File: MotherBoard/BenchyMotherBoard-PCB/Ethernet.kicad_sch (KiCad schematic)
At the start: 3 parts, among them J2 LVDS-DISPLAY, U4 AM6254ATCGGAALW, U5 SiI9022ACNU

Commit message: (WIP) Finish more of the PS schematic
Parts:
- removed J2: LVDS-DISPLAY, symbol Daxxn_Displays:Generic-Display-LVDS
- removed U4: AM6254ATCGGAALW, Daxxn_Packages:ALW0425A-BGA-425-13x13mm, symbol Daxxn_TIMicros:AM6254ATCGGAALW
- removed U5: SiI9022ACNU, Package_DFN_QFN:QFN-72-1EP_10x10mm_P0.5mm_EP6x6mm, symbol Daxxn_IC:SiI9022ACNU
- added U4: AM6254ATCGGAALW, Daxxn_Packages:ALW0425A-BGA-425-13x13mm, symbol Daxxn_TIMicros:AM6254ATCGGAALW

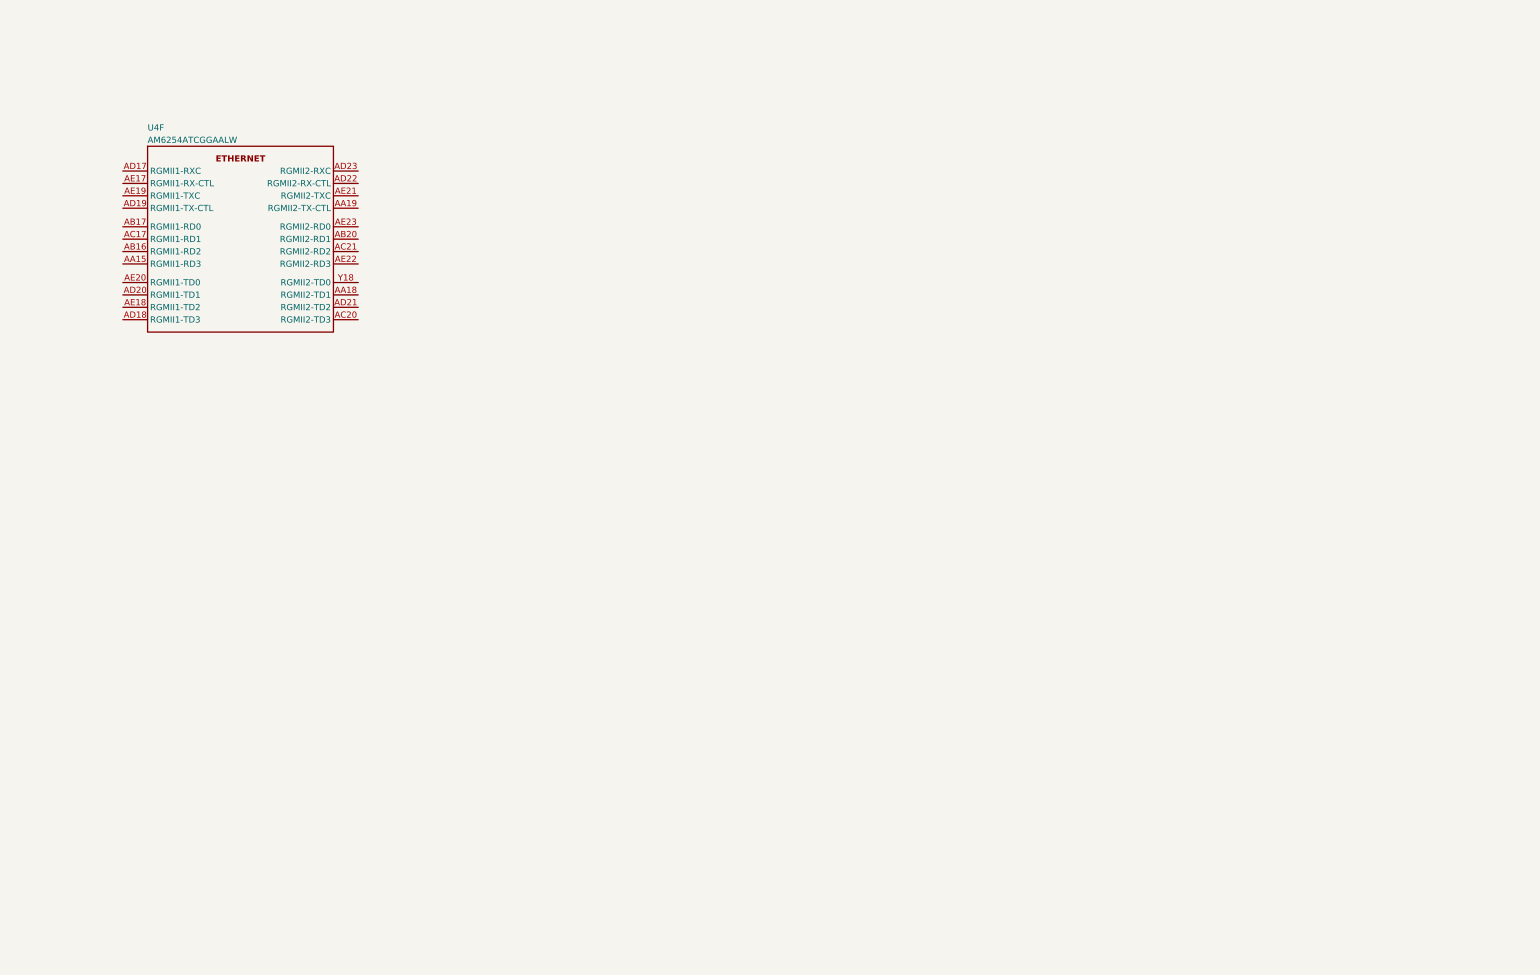
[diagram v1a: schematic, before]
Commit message: (WIP) More work on power supply sequencing
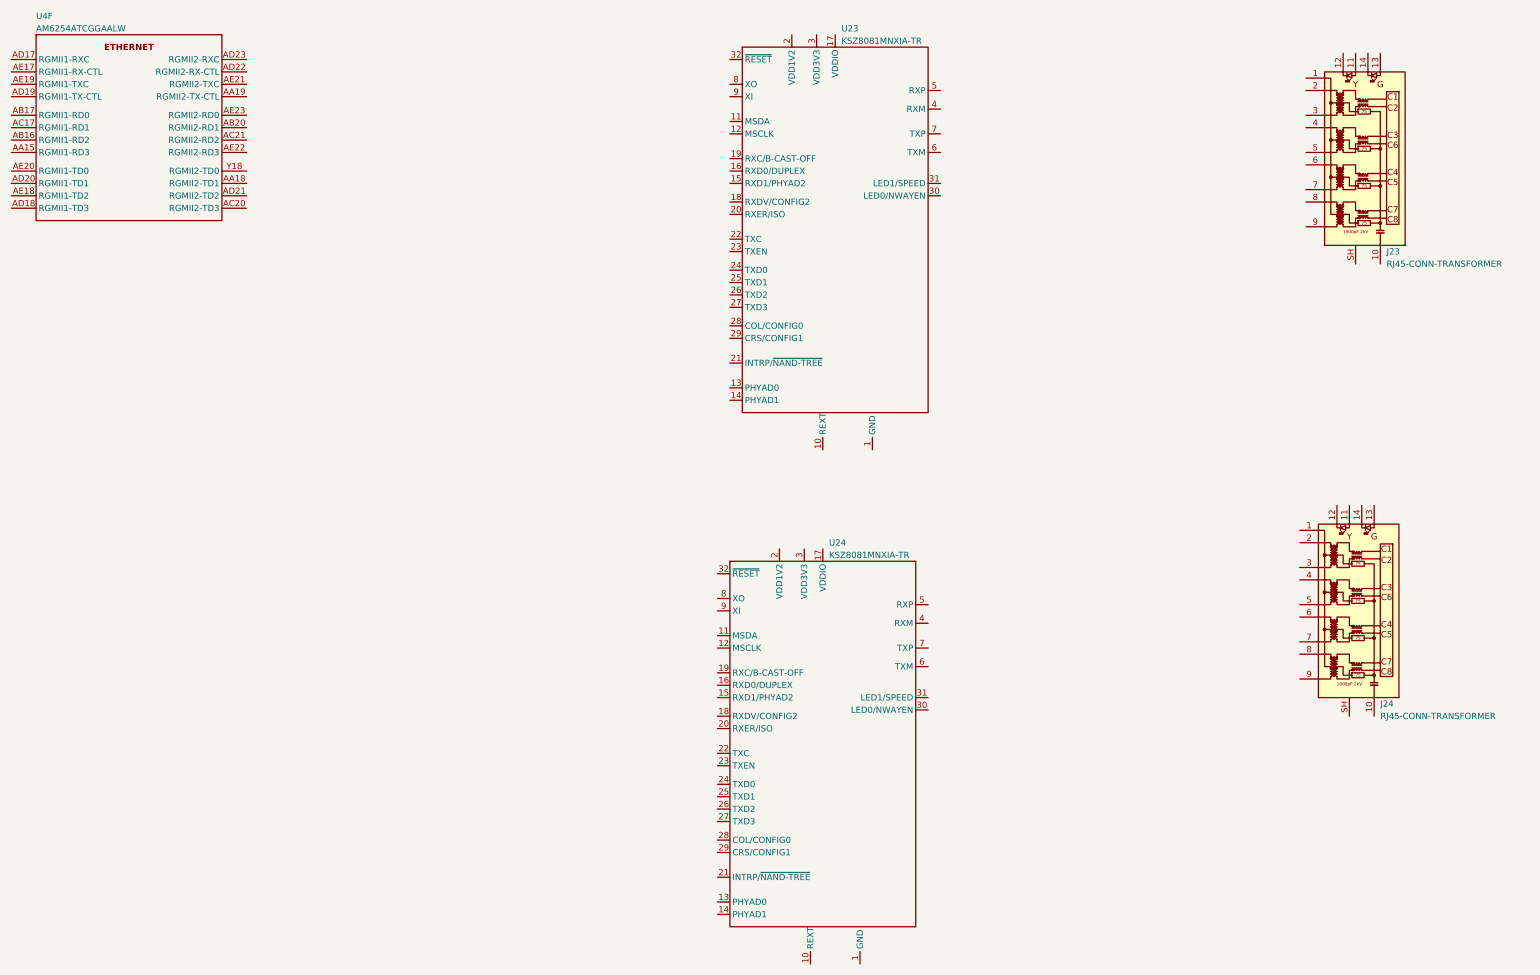
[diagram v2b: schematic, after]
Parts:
- added J23, J24: RJ45-CONN-TRANSFORMER, Daxxn_Connectors:RJ45_Wuerth_7499111446_Horizontal, symbol Daxxn_Connectors:RJ45-CONN-TRANSFORMER
- added U23, U24: KSZ8081MNXIA-TR, Package_DFN_QFN:QFN-32-1EP_5x5mm_P0.5mm_EP3.1x3.1mm, symbol Daxxn_IC:KSZ8081MNXIA-TR
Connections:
- new net GND: U23.1 (GND), U23.33 (GND), U24.1 (GND), U24.33 (GND)
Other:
- moved on the sheet: U4F
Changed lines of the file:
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@@
 (kicad_sch (version 20230121) (generator eeschema)
-  (paper "A4")
+  (paper "A3")
   (title_block
     (title "Benchy Reloaded")
@@
     (company "Daxxn Industries")
   )
-  (symbol (lib_id "Daxxn_TIMicros:AM6254ATCGGAALW") (at 58.42 44.45 0) (unit 6)
+  (symbol (lib_id "Daxxn_TIMicros:AM6254ATCGGAALW") (at 35.56 21.59 0) (unit 6)
     (in_bom yes) (on_board yes) (dnp no)
-    (property "Reference" "U4" (at 58.42 40.64 0)
-      (effects (font (size 1.27 1.27)) (justify left))
-    )
-    (property "Value" "AM6254ATCGGAALW" (at 58.42 43.18 0)
-      (effects (font (size 1.27 1.27)) (justify left))
-    )
-    (property "Footprint" "Daxxn_Packages:ALW0425A-BGA-425-13x13mm" (at 76.2 36.83 0)
-      (effects (font (size 1.27 1.27)) hide)
-    )
-    (property "Datasheet" "%LOCAL_DATASHEETS%/AM625.pdf" (at 77.47 39.37 0)
+    (property "Reference" "U4" (at 35.56 17.78 0)
+      (effects (font (size 1.27 1.27)) (justify left))
+    )
+    (property "Value" "AM6254ATCGGAALW" (at 35.56 20.32 0)
+      (effects (font (size 1.27 1.27)) (justify left))
+    )
+    (property "Footprint" "Daxxn_Packages:ALW0425A-BGA-425-13x13mm" (at 53.34 13.97 0)
+      (effects (font (size 1.27 1.27)) hide)
+    )
+    (property "Datasheet" "%LOCAL_DATASHEETS%/AM625.pdf" (at 54.61 16.51 0)
       (effects (font (size 1.27 1.27)) hide)
     )
@@
         )
       )
+    )
+  )
+  (symbol (lib_id "Daxxn_IC:KSZ8081MNXIA-TR") (at 180.34 24.13 0) (unit 1)
+    (in_bom yes) (on_board yes) (dnp no)
+    (property "Reference" "U23" (at 200.66 20.32 0)
+      (effects (font (size 1.27 1.27)) (justify left))
+    )
+    (property "Value" "KSZ8081MNXIA-TR" (at 200.66 22.86 0)
+      (effects (font (size 1.27 1.27)) (justify left))
+    )
+    (property "Footprint" "Package_DFN_QFN:QFN-32-1EP_5x5mm_P0.5mm_EP3.1x3.1mm" (at 198.12 8.89 0)
+      (effects (font (size 1.27 1.27)) hide)
+    )
+    (property "Datasheet" "%LOCAL_DATASHEETS%/KSZ8081MNX.pdf" (at 195.58 7.62 0)
+      (effects (font (size 1.27 1.27)) hide)
+    )
+    (pin "1")
+    (pin "10")
+    (pin "11")
+    (pin "12")
+    (pin "13")
+    (pin "14")
+    (pin "15")
+    (pin "16")
+    (pin "17")
+    (pin "18")
+    (pin "19")
+    (pin "2")
+    (pin "20")
+    (pin "21")
+    (pin "22")
+    (pin "23")
+    (pin "24")
+    (pin "25")
+    (pin "26")
+    (pin "27")
+    (pin "28")
+    (pin "29")
+    (pin "3")
+    (pin "30")
+    (pin "31")
+    (pin "32")
+    (pin "33")
+    (pin "4")
+    (pin "5")
+    (pin "6")
+    (pin "7")
+    (pin "8")
+    (pin "9")
+    (instances
+      (project "BenchyMotherBoard-PCB"
+        (path "/2ea077fe-b0e6-467f-a1c1-8336ebdb7a86/3f394e38-756b-4eaa-ba31-47b873a984c7"
+          (reference "U23") (unit 1)
+        )
+      )
+    )
+  )
+  (symbol (lib_id "Daxxn_Connectors:RJ45-CONN-TRANSFORMER") (at 306.07 140.97 0) (unit 1)
+    (in_bom yes) (on_board yes) (dnp no)
+    (property "Reference" "J24" (at 311.15 158.75 0)
+      (effects (font (size 1.27 1.27)) (justify left))
+    )
+    (property "Value" "RJ45-CONN-TRANSFORMER" (at 311.15 161.29 0)
+      (effects (font (size 1.27 1.27)) (justify left))
+    )
+    (property "Footprint" "Daxxn_Connectors:RJ45_Wuerth_7499111446_Horizontal" (at 306.07 110.49 0)
+      (effects (font (size 1.27 1.27)) hide)
+    )
+    (property "Datasheet" "%DRAWINGS%/Connectors/7499111446.pdf" (at 306.07 106.68 0)
+      (effects (font (size 1.27 1.27)) (justify top) hide)
+    )
+    (pin "10")
+    (pin "1")
+    (pin "11")
+    (pin "12")
+    (pin "13")
+    (pin "14")
+    (pin "2")
+    (pin "3")
+    (pin "4")
+    (pin "5")
+    (pin "6")
+    (pin "7")
+    (pin "8")
+    (pin "9")
+    (pin "SH")
+    (instances
+      (project "BenchyMotherBoard-PCB"
+        (path "/2ea077fe-b0e6-467f-a1c1-8336ebdb7a86/3f394e38-756b-4eaa-ba31-47b873a984c7"
+          (reference "J24") (unit 1)
+        )
+      )
+    )
+  )
+  (symbol (lib_id "Daxxn_Connectors:RJ45-CONN-TRANSFORMER") (at 307.34 48.26 0) (unit 1)
+    (in_bom yes) (on_board yes) (dnp no)
+    (property "Reference" "J23" (at 312.42 66.04 0)
+      (effects (font (size 1.27 1.27)) (justify left))
+    )
+    (property "Value" "RJ45-CONN-TRANSFORMER" (at 312.42 68.58 0)
+      (effects (font (size 1.27 1.27)) (justify left))
+    )
+    (property "Footprint" "Daxxn_Connectors:RJ45_Wuerth_7499111446_Horizontal" (at 307.34 17.78 0)
+      (effects (font (size 1.27 1.27)) hide)
+    )
+    (property "Datasheet" "%DRAWINGS%/Connectors/7499111446.pdf" (at 307.34 13.97 0)
+      (effects (font (size 1.27 1.27)) (justify top) hide)
+    )
+    (pin "10")
+    (pin "1")
+    (pin "11")
+    (pin "12")
+    (pin "13")
+    (pin "14")
+    (pin "2")
+    (pin "3")
+    (pin "4")
+    (pin "5")
+    (pin "6")
+    (pin "7")
+    (pin "8")
+    (pin "9")
+    (pin "SH")
+    (instances
+      (project "BenchyMotherBoard-PCB"
+        (path "/2ea077fe-b0e6-467f-a1c1-8336ebdb7a86/3f394e38-756b-4eaa-ba31-47b873a984c7"
+          (reference "J23") (unit 1)
+        )
+      )
+    )
+  )
+  (symbol (lib_id "Daxxn_IC:KSZ8081MNXIA-TR") (at 177.8 129.54 0) (unit 1)
+    (in_bom yes) (on_board yes) (dnp no)
+    (property "Reference" "U24" (at 198.12 125.73 0)
+      (effects (font (size 1.27 1.27)) (justify left))
+    )
+    (property "Value" "KSZ8081MNXIA-TR" (at 198.12 128.27 0)
+      (effects (font (size 1.27 1.27)) (justify left))
+    )
+    (property "Footprint" "Package_DFN_QFN:QFN-32-1EP_5x5mm_P0.5mm_EP3.1x3.1mm" (at 195.58 114.3 0)
+      (effects (font (size 1.27 1.27)) hide)
+    )
+    (property "Datasheet" "%LOCAL_DATASHEETS%/KSZ8081MNX.pdf" (at 193.04 113.03 0)
+      (effects (font (size 1.27 1.27)) hide)
+    )
+    (pin "1")
+    (pin "10")
+    (pin "11")
+    (pin "12")
+    (pin "13")
+    (pin "14")
+    (pin "15")
+    (pin "16")
+    (pin "17")
+    (pin "18")
+    (pin "19")
+    (pin "2")
+    (pin "20")
+    (pin "21")
+    (pin "22")
+    (pin "23")
+    (pin "24")
+    (pin "25")
+    (pin "26")
+    (pin "27")
+    (pin "28")
+    (pin "29")
+    (pin "3")
+    (pin "30")
+    (pin "31")
+    (pin "32")
+    (pin "33")
+    (pin "4")
+    (pin "5")
+    (pin "6")
+    (pin "7")
+    (pin "8")
+    (pin "9")
+    (instances
+      (project "BenchyMotherBoard-PCB"
+        (path "/2ea077fe-b0e6-467f-a1c1-8336ebdb7a86/3f394e38-756b-4eaa-ba31-47b873a984c7"
+          (reference "U24") (unit 1)
+        )
+      )

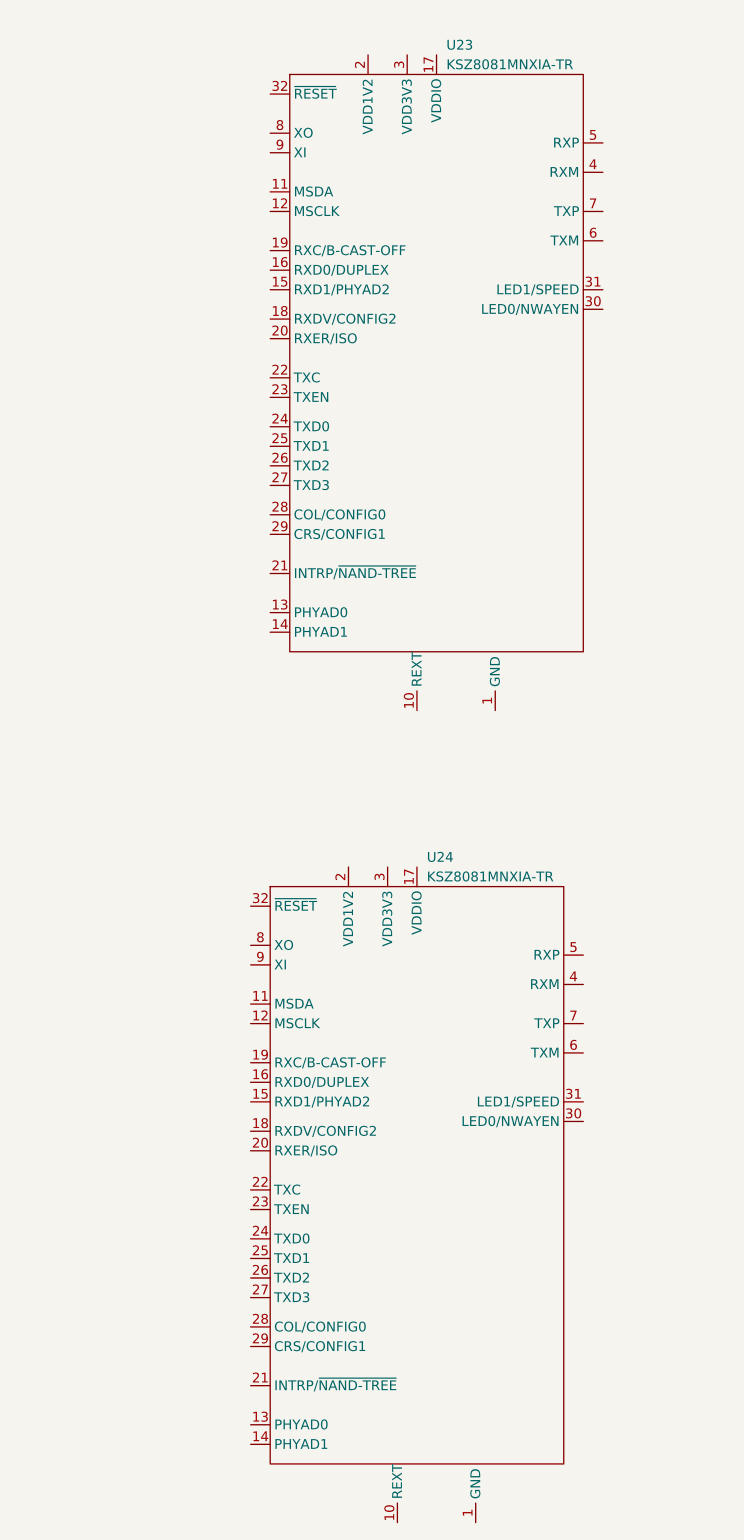
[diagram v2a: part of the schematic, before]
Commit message: (WIP) Complete most of the PS and boot schematics
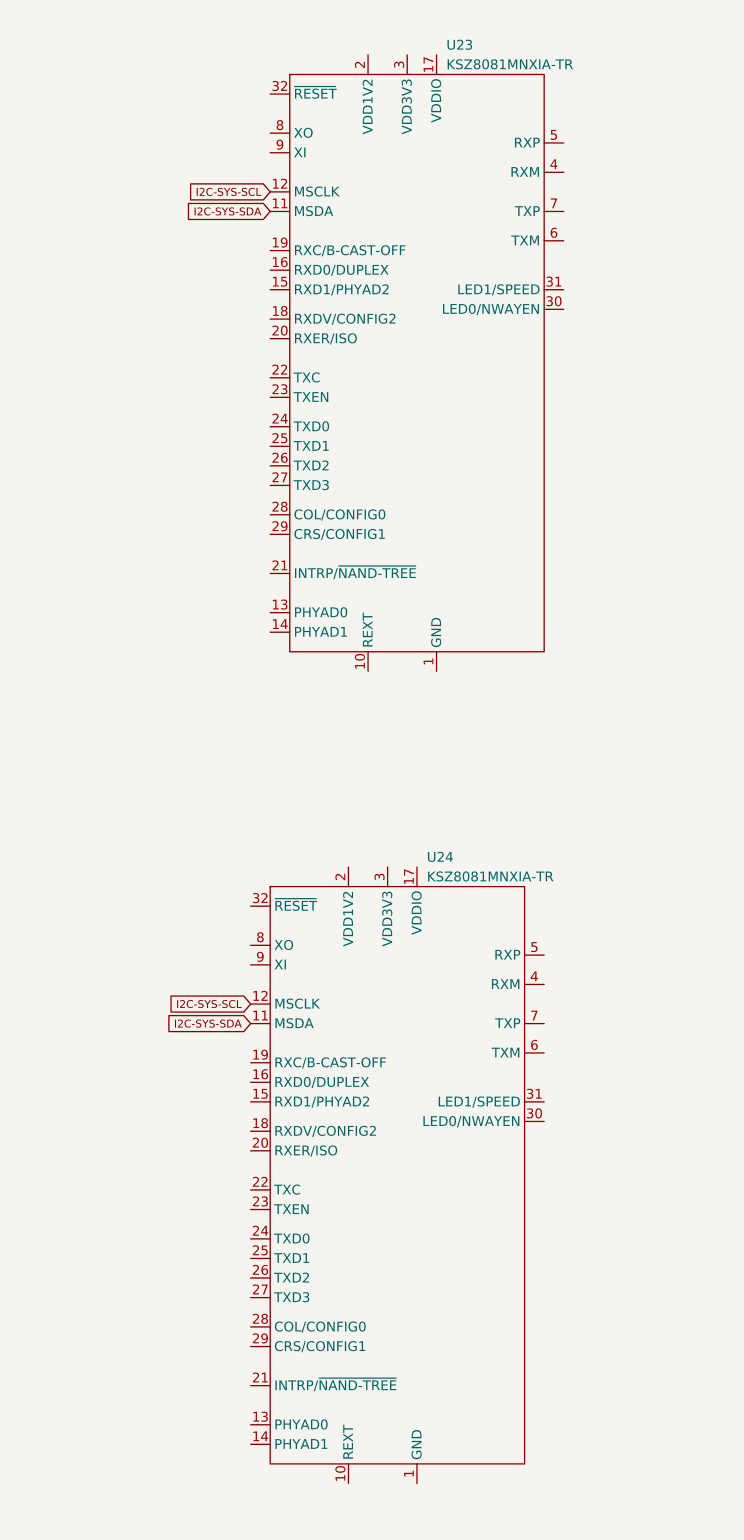
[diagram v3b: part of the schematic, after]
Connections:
- net I2C-SYS-SDA: now reaches U23.11 (MSDA)
- net I2C-SYS-SDA: now also U24.11 (MSDA)
- net I2C-SYS-SCL: now reaches U23.12 (MSCLK)
- net I2C-SYS-SCL: now also U24.12 (MSCLK)
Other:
- moved on the sheet: U23, U24
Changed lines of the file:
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@@
     (company "Daxxn Industries")
+  )
+  (global_label "I2C-SYS-SCL" (shape input) (at 175.26 144.78 180) (fields_autoplaced)
+    (effects (font (size 1.016 1.016)) (justify right))
+    (property "Intersheetrefs" "${INTERSHEET_REFS}" (at 162.3401 144.78 0)
+      (effects (font (size 1.27 1.27)) (justify right))
+    )
+  )
+  (global_label "I2C-SYS-SCL" (shape input) (at 177.8 39.37 180) (fields_autoplaced)
+    (effects (font (size 1.016 1.016)) (justify right))
+    (property "Intersheetrefs" "${INTERSHEET_REFS}" (at 164.8801 39.37 0)
+      (effects (font (size 1.27 1.27)) (justify right))
+    )
+  )
+  (global_label "I2C-SYS-SDA" (shape input) (at 175.26 147.32 180) (fields_autoplaced)
+    (effects (font (size 1.016 1.016)) (justify right))
+    (property "Intersheetrefs" "${INTERSHEET_REFS}" (at 162.2917 147.32 0)
+      (effects (font (size 1.27 1.27)) (justify right))
+    )
+  )
+  (global_label "I2C-SYS-SDA" (shape input) (at 177.8 41.91 180) (fields_autoplaced)
+    (effects (font (size 1.016 1.016)) (justify right))
+    (property "Intersheetrefs" "${INTERSHEET_REFS}" (at 164.8317 41.91 0)
+      (effects (font (size 1.27 1.27)) (justify right))
+    )
   )
   (symbol (lib_id "Daxxn_TIMicros:AM6254ATCGGAALW") (at 35.56 21.59 0) (unit 6)
@@
     )
     (property "Datasheet" "%LOCAL_DATASHEETS%/AM625.pdf" (at 54.61 16.51 0)
+      (effects (font (size 1.27 1.27)) hide)
+    )
+    (property "Schematic" "" (at 35.56 21.59 0)
+      (effects (font (size 1.27 1.27)) hide)
+    )
+    (property "PartNumber" "" (at 35.56 21.59 0)
+      (effects (font (size 1.27 1.27)))
+    )
+    (property "SupplierPN" "" (at 35.56 21.59 0)
       (effects (font (size 1.27 1.27)) hide)
     )
@@
       (effects (font (size 1.27 1.27)) hide)
     )
+    (property "Schematic" "" (at 180.34 24.13 0)
+      (effects (font (size 1.27 1.27)) hide)
+    )
+    (property "PartNumber" "" (at 180.34 24.13 0)
+      (effects (font (size 1.27 1.27)))
+    )
+    (property "SupplierPN" "" (at 180.34 24.13 0)
+      (effects (font (size 1.27 1.27)) hide)
+    )
